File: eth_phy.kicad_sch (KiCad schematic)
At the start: 32 parts, among them U3 DP83TC812RRHARQ1

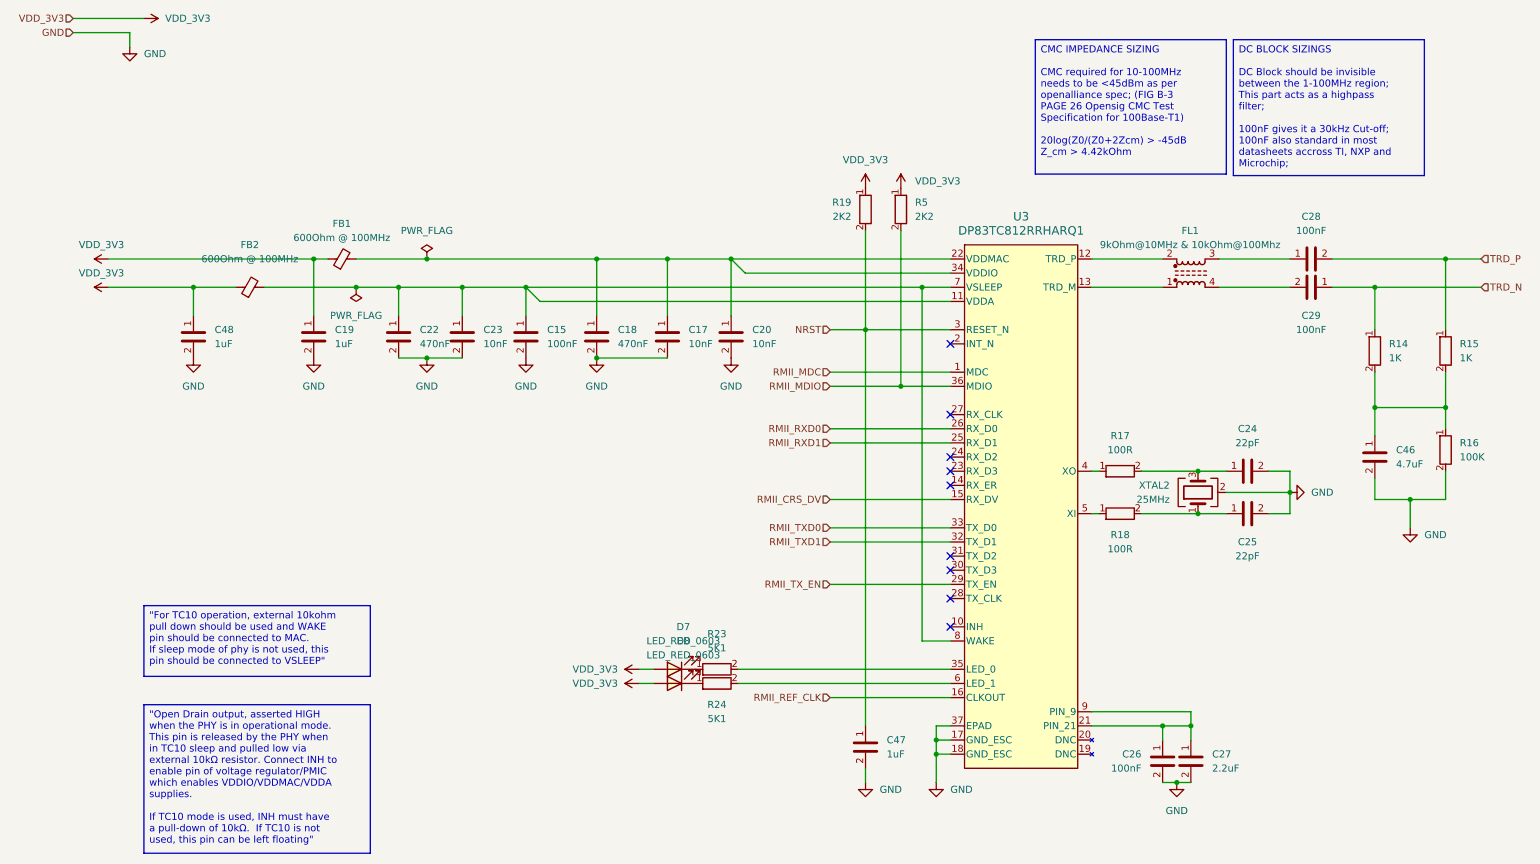
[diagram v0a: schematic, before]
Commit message: feat: implmeneted revamp with normal ethernet LAN8742A
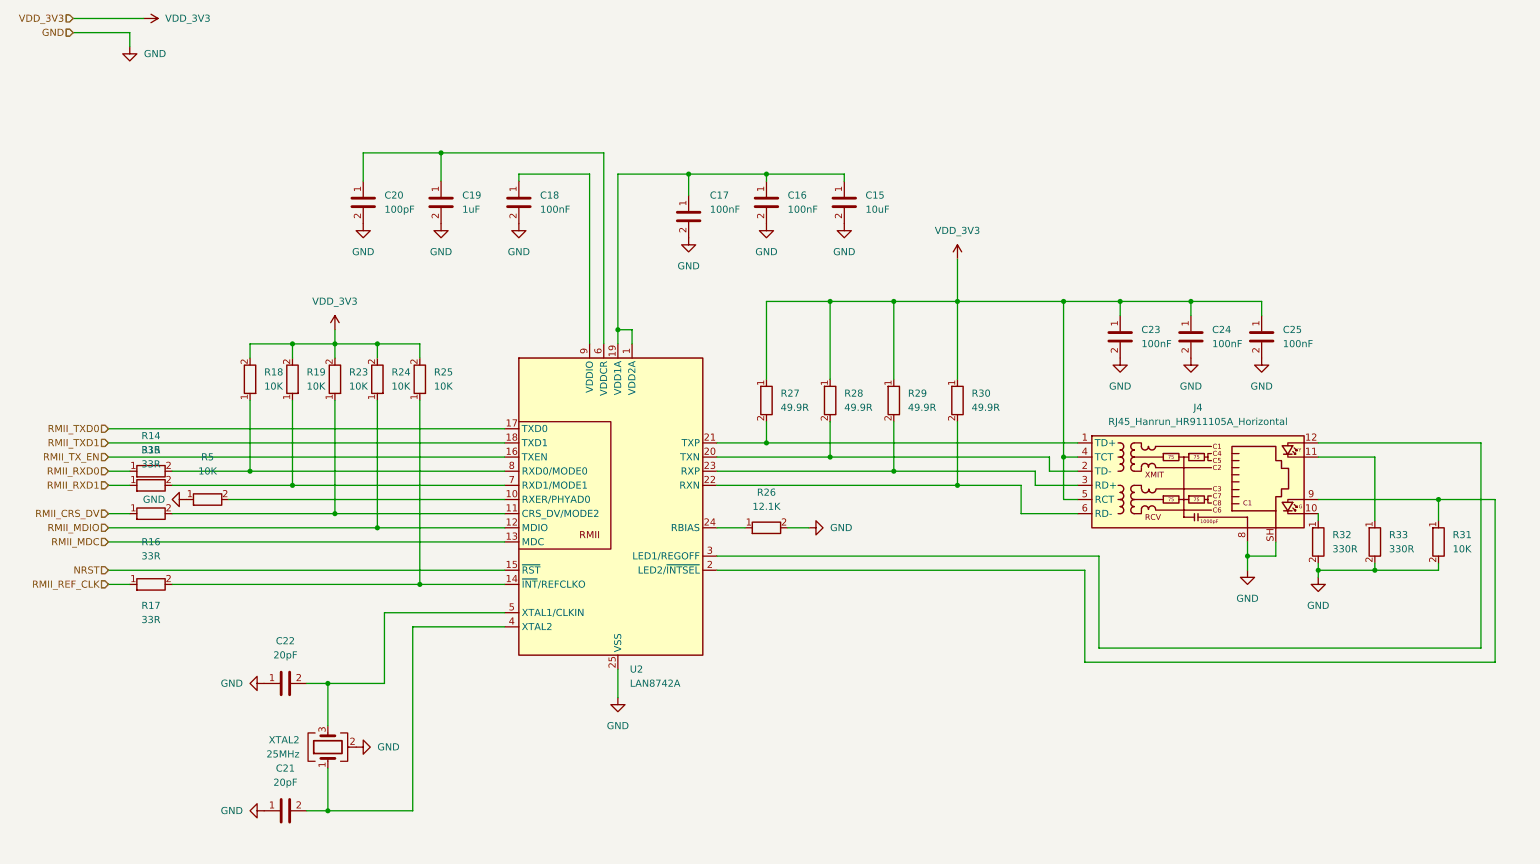
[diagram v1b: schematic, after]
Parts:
- removed C15, C26, C28, C29: 100nF, chenry-footprint-lib:C_0402, symbol 0_chenry_lib:C_0402_100N
- removed C17, C20, C23: 10nF, chenry-footprint-lib:C_0402, symbol 0_chenry_lib:C_0402_10N
- removed C18, C22: 470nF, chenry-footprint-lib:C_0402, symbol 0_chenry_lib:C_0402_470N
- removed C19, C47, C48: 1uF, chenry-footprint-lib:C_0402, symbol 0_chenry_lib:C_0402_1U
- removed C24, C25: 22pF, chenry-footprint-lib:C_0402, symbol 0_chenry_lib:C_0402_22P
- removed C27: 2.2uF, chenry-footprint-lib:C_0402, symbol 0_chenry_lib:C_0402_2U2
- removed C46: 4.7uF, chenry-footprint-lib:C_0402, symbol 0_chenry_lib:C_0402_4N7
- removed D7, D8: LED_RED_0603, LED_SMD:LED_0603_1608Metric, symbol 0_chenry_lib:LED_RED_0603
- removed FB1, FB2: 600Ohm @ 100MHz, Capacitor_SMD:C_0603_1608Metric, symbol 0_chenry_lib:BLM18KG601SH
- removed FL1: 9kOhm@10MHz & 10kOhm@100Mhz, Inductor_SMD:L_CommonModeChoke_Coilank_ACM3225, symbol 0_chenry_lib:ACT1210L-201
- removed R14, R15: 1K, chenry-footprint-lib:R_0402, symbol 0_chenry_lib:R_0402_1K
- removed R16: 100K, chenry-footprint-lib:R_0402, symbol 0_chenry_lib:R_0402_100K
- removed R17, R18: 100R, chenry-footprint-lib:R_0402, symbol 0_chenry_lib:R_0402_100
- removed R19, R5: 2K2, chenry-footprint-lib:R_0402, symbol 0_chenry_lib:R_0402_2K2
- removed R23, R24: 5K1, chenry-footprint-lib:R_0402, symbol 0_chenry_lib:R_0402_5K1
- removed U3: DP83TC812RRHARQ1, chenry-footprint-lib:VQFN36_RHA_TEX, symbol 0_chenry_lib:DP83TC812RRHARQ1
- removed XTAL2: 25MHz, Crystal:Crystal_SMD_3225-4Pin_3.2x2.5mm, symbol 0_chenry_lib:X322525MOB4SI
- added C15: 10uF, chenry-footprint-lib:C_0402, symbol 0_chenry-lib:C_0402_10U
- added C16, C17, C18, C23, C24, C25: 100nF, chenry-footprint-lib:C_0402, symbol 0_chenry-lib:C_0402_100N
- added C19: 1uF, chenry-footprint-lib:C_0402, symbol 0_chenry-lib:C_0402_1U
- added C20: 100pF, chenry-footprint-lib:C_0402, symbol 0_chenry-lib:C_0402_100P
- added C21, C22: 20pF, chenry-footprint-lib:C_0402, symbol 0_chenry-lib:C_0402_20P
- added J4: RJ45_Hanrun_HR911105A_Horizontal, chenry-footprint-lib:RJ45_Hanrun_HR911105A_Horizontal, symbol 0_chenry-lib:RJ45_Hanrun_HR911105A_Horizontal
- added R14, R15, R16, R17: 33R, chenry-footprint-lib:R_0402, symbol 0_chenry-lib:R_0402_33R
- added R18, R19, R23, R24, R25, R31, R5: 10K, chenry-footprint-lib:R_0402, symbol 0_chenry-lib:R_0402_10K
- added R26: 12.1K, chenry-footprint-lib:R_0402, symbol 0_chenry-lib:R_0402_12K1
- added R27, R28, R29, R30: 49.9R, chenry-footprint-lib:R_0402, symbol 0_chenry-lib:R_0402_49R9
- added R32, R33: 330R, chenry-footprint-lib:R_0402, symbol 0_chenry-lib:R_0402_330R
- added U2: LAN8742A, chenry-footprint-lib:VQFN-24-1EP_4x4mm_P0.5mm_EP2.5x2.5mm_ThermalVias, symbol 0_chenry-lib:LAN8742A
- added XTAL2: 25MHz, Crystal:Crystal_SMD_3225-4Pin_3.2x2.5mm, symbol 0_chenry-lib:X322525MOB4SI
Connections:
- net GND: now also C15.2, C16.2, C17.2, C18.2, C19.2, C20.2, C21.1, C22.1, C23.2, C24.2, C25.2, J4.8, J4.SH, R26.2, R31.2, R32.2, R33.2, R5.1, U2.25 (VSS), XTAL2.2 (G), XTAL2.4 (G)
- net NRST: now also U2.15 (~{RST})
- net RMII_CRS_DV: now also R16.1
- net RMII_MDC: now also U2.13 (MDC)
- net RMII_MDIO: now also R24.1, U2.12 (MDIO)
- net RMII_REF_CLK: now also R17.1
- net RMII_RXD0: now also R14.1
- net RMII_RXD1: now also R15.1
- net RMII_TXD0: now also U2.17 (TXD0)
- net RMII_TXD1: now also U2.18 (TXD1)
- net RMII_TX_EN: now also U2.16 (TXEN)
- net VDD_3V3: now also C23.1, C24.1, C25.1, J4.4 (TCT), J4.5 (RCT), R18.2, R19.2, R23.2, R24.2, R25.2, R27.1, R28.1, R29.1, R30.1
- new net: R15.2, R19.1, U2.7 (RXD1/MODE1)
- new net: C19.1, C20.1, U2.6 (VDDCR)
- new net: R5.2, U2.10 (RXER/PHYAD0)
- new net: J4.10, R32.1
- new net: J4.1 (TD+), R27.2, U2.21 (TXP)
- new net: J4.3 (RD+), R29.2, U2.23 (RXP)
- new net: R14.2, R18.1, U2.8 (RXD0/MODE0)
- new net: R16.2, R23.1, U2.11 (CRS_DV/MODE2)
- new net: C18.1, U2.9 (VDDIO)
- new net: R17.2, R25.1, U2.14 (~{INT}/REFCLKO)
- new net: C15.1, C16.1, C17.1, U2.1 (VDD2A), U2.19 (VDD1A)
- new net: J4.9, R31.1, U2.2 (LED2/~{INTSEL})
- new net: J4.2 (TD-), R28.2, U2.20 (TXN)
- new net: J4.6 (RD-), R30.2, U2.22 (RXN)
- new net: R26.1, U2.24 (RBIAS)
- new net: J4.12, U2.3 (LED1/REGOFF)
- new net: C21.2, U2.4 (XTAL2), XTAL2.1
- new net: C22.2, U2.5 (XTAL1/CLKIN), XTAL2.3
- new net: J4.11, R33.1
- no-connect marks 9 -> 0

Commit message: fix(eth_phy): completed revamp with lan8742a
BREAKING CHANGE:
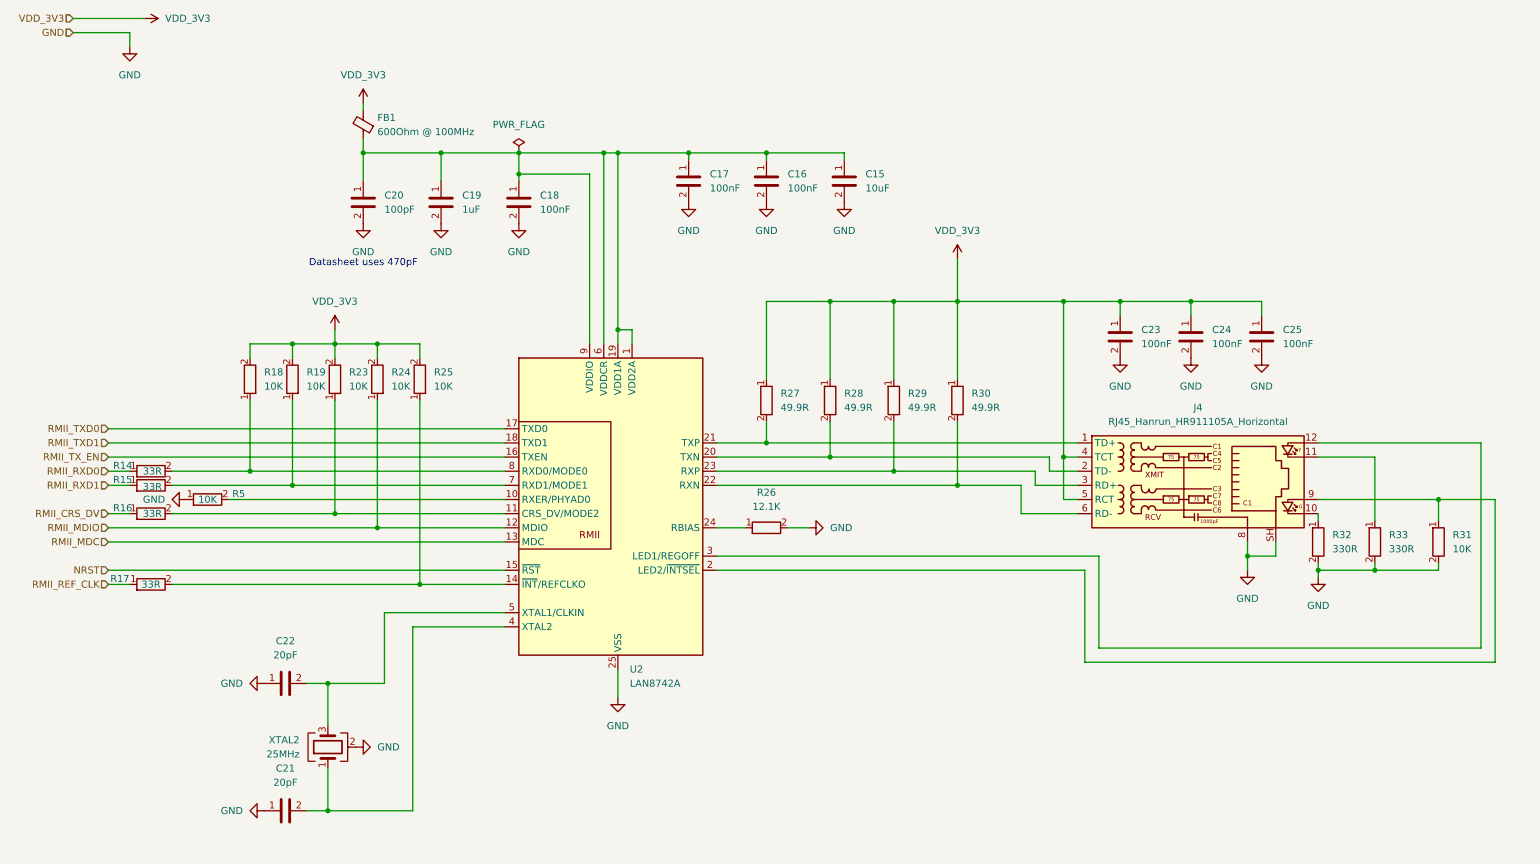
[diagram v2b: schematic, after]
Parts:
- added FB1: 600Ohm @ 100MHz, Capacitor_SMD:C_0603_1608Metric, symbol 0_chenry_lib:BLM18KG601SH
- C15: symbol 0_chenry-lib:C_0402_10U -> 0_chenry_lib:C_0402_10U
- C16, C17, C18, C23, C24, C25: symbol 0_chenry-lib:C_0402_100N -> 0_chenry_lib:C_0402_100N
- C19: symbol 0_chenry-lib:C_0402_1U -> 0_chenry_lib:C_0402_1U
- C20: symbol 0_chenry-lib:C_0402_100P -> 0_chenry_lib:C_0402_100P
- C21, C22: symbol 0_chenry-lib:C_0402_20P -> 0_chenry_lib:C_0402_20P
- J4: symbol 0_chenry-lib:RJ45_Hanrun_HR911105A_Horizontal -> 0_chenry_lib:RJ45_Hanrun_HR911105A_Horizontal
- R14, R15, R16, R17: symbol 0_chenry-lib:R_0402_33R -> 0_chenry_lib:R_0402_33R
- R18, R19, R23, R24, R25, R31, R5: symbol 0_chenry-lib:R_0402_10K -> 0_chenry_lib:R_0402_10K
- R26: symbol 0_chenry-lib:R_0402_12K1 -> 0_chenry_lib:R_0402_12K1
- R27, R28, R29, R30: symbol 0_chenry-lib:R_0402_49R9 -> 0_chenry_lib:R_0402_49R9
- R32, R33: symbol 0_chenry-lib:R_0402_330R -> 0_chenry_lib:R_0402_330R
- U2: symbol 0_chenry-lib:LAN8742A -> 0_chenry_lib:LAN8742A
- XTAL2: symbol 0_chenry-lib:X322525MOB4SI -> 0_chenry_lib:X322525MOB4SI
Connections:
- net VDD_3V3: now also FB1.2
- net at C19.1, C20.1, U2.6 (VDDCR): now also C15.1, C16.1, C17.1, C18.1, U2.1 (VDD2A), U2.19 (VDD1A), U2.9 (VDDIO), FB1.1
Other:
- note added: "Datasheet uses 470pF"
- moved on the sheet: C15, C16, C17
